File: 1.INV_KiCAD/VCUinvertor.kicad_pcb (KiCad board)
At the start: 2 copper layers, 100.7 x 138.5 mm, 160 parts, among them J10 FAN2, J11 PUMP1, J12 PUMP2, J7 PowerSupply, J8 FAN1, J9 BRAKE LIGHT, K1 IM06DGR, Q1 2N7002, Q10 2N7002, Q11 2N7002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

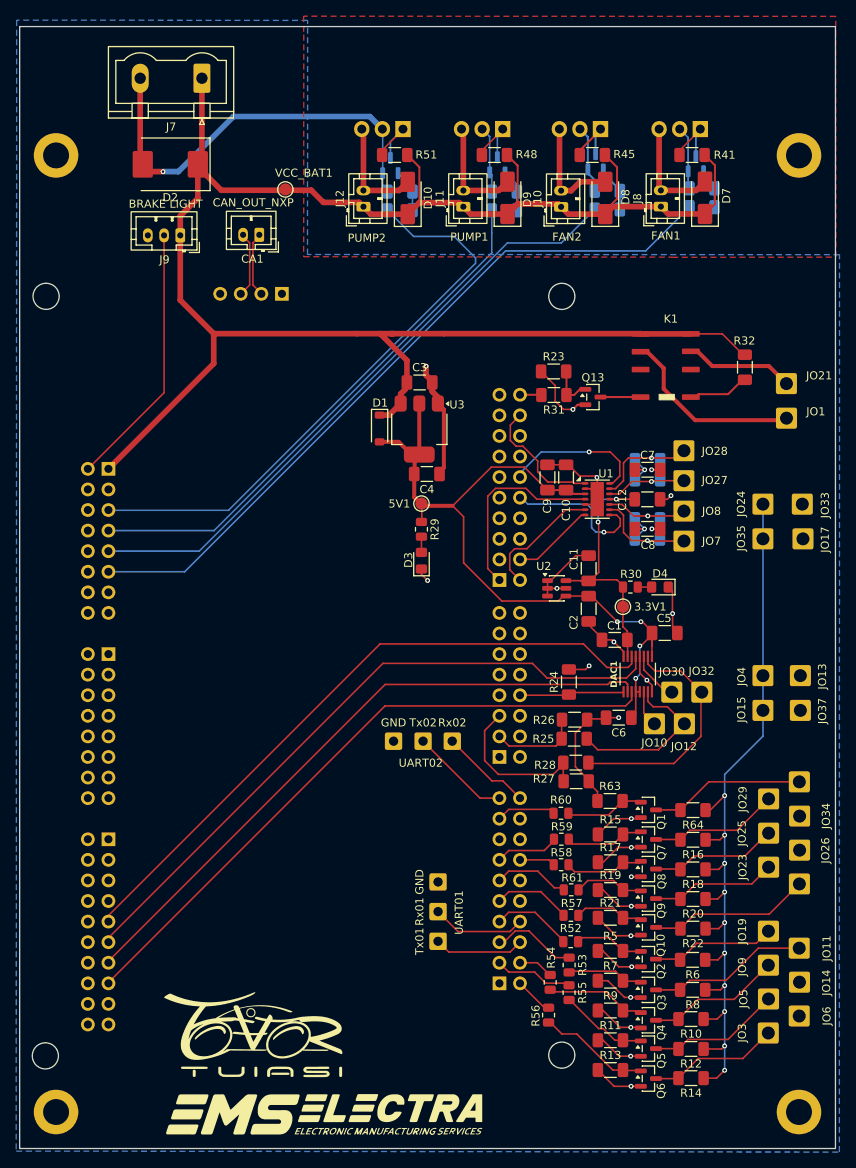
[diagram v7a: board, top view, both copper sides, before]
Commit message: Board silkscreen corrections for visibility
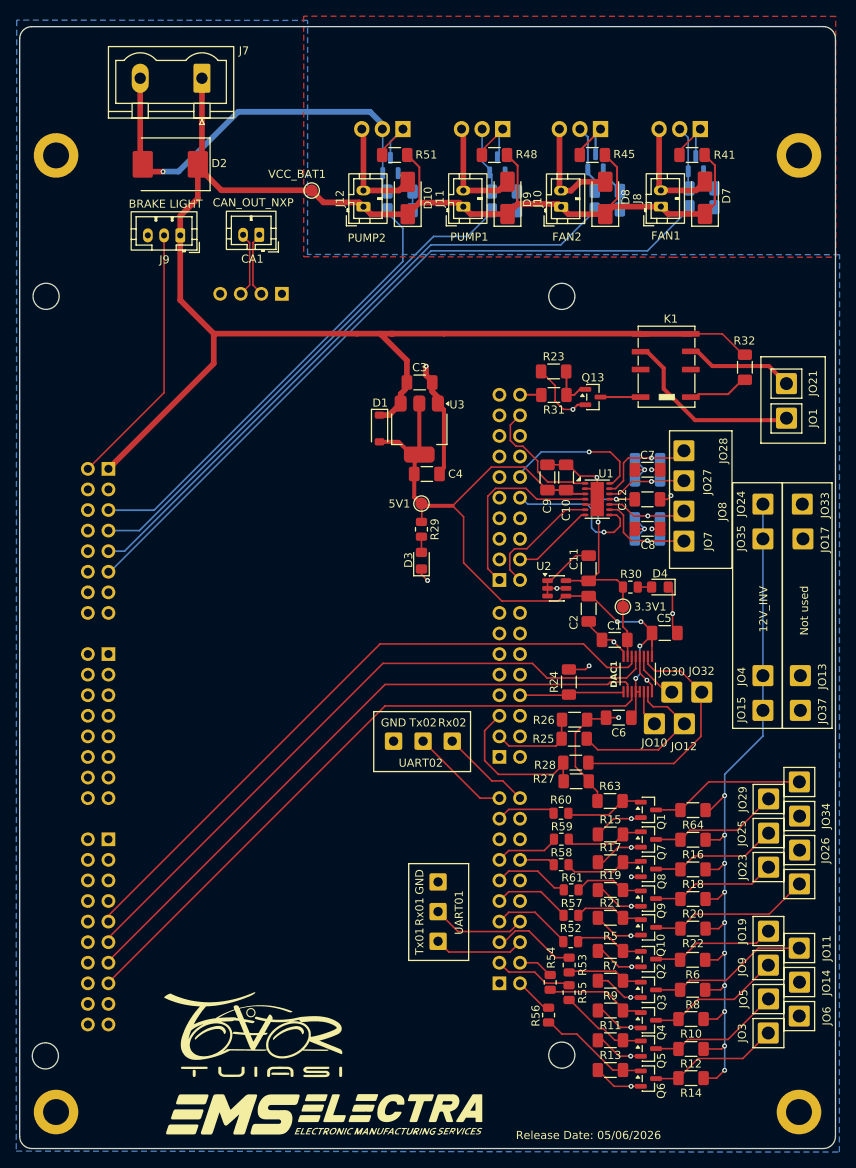
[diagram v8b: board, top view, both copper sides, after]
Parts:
- moved VCC_BAT1 3.25 mm to (88.1, 48.7)
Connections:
- net /INV1_VCC renamed /INV1_Vcc
- net /INV2_VCC renamed /INV2_Vcc
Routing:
- net /PUMP2: track 71.9 -> 56.2 mm
- net /PUMP1: track 66.8 -> 63.8 mm
- net GND: track 226.4 -> 227.2 mm
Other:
- outline, holes or cut-outs redrawn
- board text added: "Release Date: 05/06/2026"
